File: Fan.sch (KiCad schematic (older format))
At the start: 17 parts, among them Q2 DMN65D8L-7, Q3 AOD476, Q4 AOD476, U11 OPA4170, U8 MCP4801

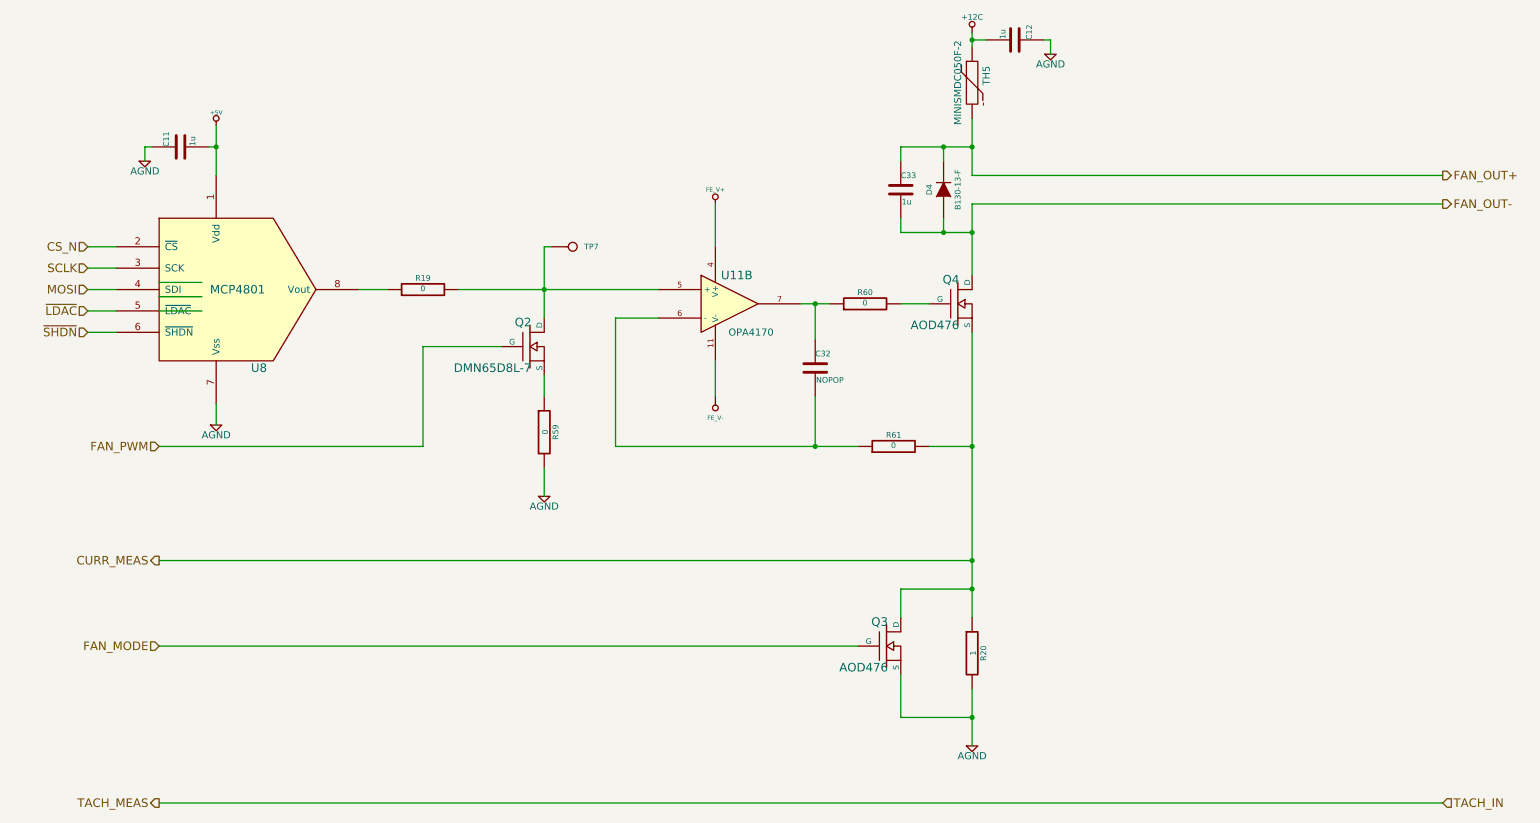
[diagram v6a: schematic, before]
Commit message: Final part numbers added to schematic, cross-checked KiCAD BOM against manual BOM
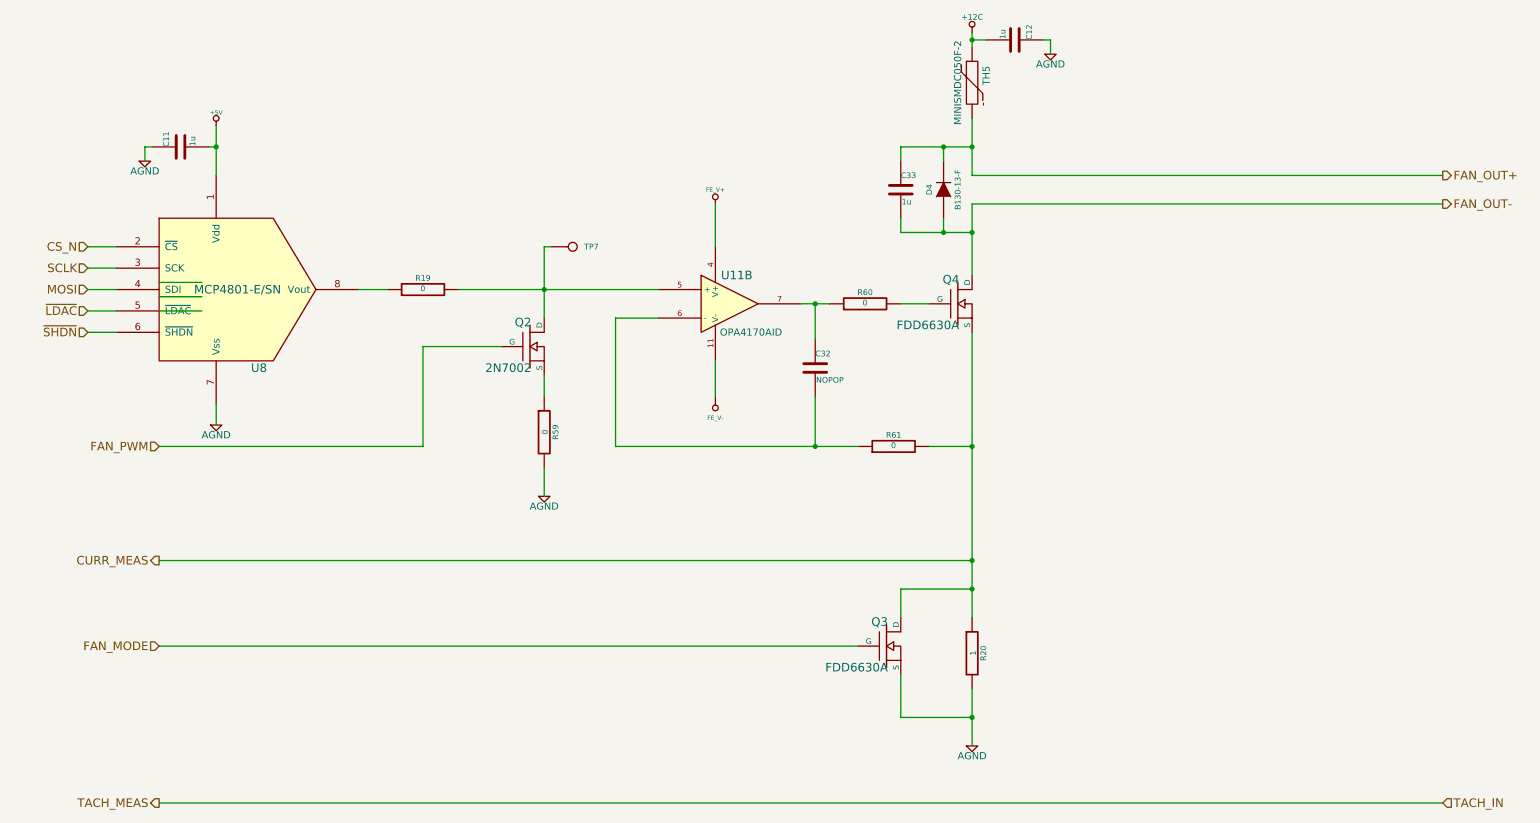
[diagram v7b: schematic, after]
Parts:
- Q2: value DMN65D8L-7 -> 2N7002
- Q3, Q4: value AOD476 -> FDD6630A
- U11: value OPA4170 -> OPA4170AID
- U8: value MCP4801 -> MCP4801-E/SN
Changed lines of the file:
@@
 P 5500 2600
 F 0 "U11" H 5550 2800 60  0000 C CNN
-F 1 "OPA4170" H 5650 2400 50  0000 C CNN
+F 1 "OPA4170AID" H 5650 2400 50  0000 C CNN
 F 2 "SMD_Packages:SO14E" H 5500 2600 60  0001 C CNN
 F 3 "" H 5500 2600 60  0000 C CNN
@@
 P 1900 2500
 F 0 "U8" H 2200 1950 60  0000 C CNN
-F 1 "MCP4801" H 2050 2500 60  0000 C CNN
+F 1 "MCP4801-E/SN" H 2050 2500 60  0000 C CNN
 F 2 "SMD_Packages:SO8N" H 1900 2500 60  0001 C CNN
 F 3 "" H 1900 2500 60  0000 C CNN
@@
 P 7100 2600
 F 0 "Q4" H 7110 2770 60  0000 R CNN
-F 1 "AOD476" H 7110 2450 60  0000 R CNN
+F 1 "FDD6630A" H 7110 2450 60  0000 R CNN
 F 2 "SMD_Packages:DPAK2" H 7100 2600 60  0001 C CNN
 F 3 "" H 7100 2600 60  0000 C CNN
@@
 P 6600 5000
 F 0 "Q3" H 6610 5170 60  0000 R CNN
-F 1 "AOD476" H 6610 4850 60  0000 R CNN
+F 1 "FDD6630A" H 6610 4850 60  0000 R CNN
 F 2 "SMD_Packages:DPAK2" H 6600 5000 60  0001 C CNN
 F 3 "" H 6600 5000 60  0000 C CNN
@@
 P 4100 2900
 F 0 "Q2" H 4110 3070 60  0000 R CNN
-F 1 "DMN65D8L-7" H 4110 2750 60  0000 R CNN
+F 1 "2N7002" H 4110 2750 60  0000 R CNN
 F 2 "SMD_Packages:SOT23EBC" H 4100 2900 60  0001 C CNN
 F 3 "" H 4100 2900 60  0000 C CNN
